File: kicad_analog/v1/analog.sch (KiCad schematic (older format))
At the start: 9 parts, among them J1 Conn_01x03, J2 Conn_02x05_Odd_Even, J3 Conn_02x05_Odd_Even, U1 BH2220FVM, U2 TSV994, U3 TSV994

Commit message: Add rough layout of components for 3d pcb view
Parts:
- J2: footprint Connector_PinSocket_2.54mm:PinSocket_2x05_P2.54mm_Vertical -> Connector_PinHeader_2.54mm:PinHeader_2x05_P2.54mm_Horizontal
- J3: footprint Connector_PinSocket_2.54mm:PinSocket_2x05_P2.54mm_Vertical -> Connector_PinSocket_2.54mm:PinSocket_2x05_P2.54mm_Horizontal
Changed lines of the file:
@@
 F 0 "J2" H 2150 3567 50  0000 C CNN
 F 1 "Conn_02x05_Odd_Even" H 2150 3476 50  0000 C CNN
-F 2 "Connector_PinSocket_2.54mm:PinSocket_2x05_P2.54mm_Vertical" H 2100 3150 50  0001 C CNN
+F 2 "Connector_PinHeader_2.54mm:PinHeader_2x05_P2.54mm_Horizontal" H 2100 3150 50  0001 C CNN
 F 3 "~" H 2100 3150 50  0001 C CNN
 	1    2100 3150
@@
 F 0 "J3" H 10100 3667 50  0000 C CNN
 F 1 "Conn_02x05_Odd_Even" H 10100 3576 50  0000 C CNN
-F 2 "Connector_PinSocket_2.54mm:PinSocket_2x05_P2.54mm_Vertical" H 10050 3250 50  0001 C CNN
+F 2 "Connector_PinSocket_2.54mm:PinSocket_2x05_P2.54mm_Horizontal" H 10050 3250 50  0001 C CNN
 F 3 "~" H 10050 3250 50  0001 C CNN
 	1    10050 3250

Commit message: Analog board updated with MAX9201, terminators and rough pcb layout
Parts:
- removed J2: Conn_02x05_Odd_Even, Connector_PinHeader_2.54mm:PinHeader_2x05_P2.54mm_Horizontal, symbol Connector_Generic:Conn_02x05_Odd_Even
- removed U2, U3: TSV994, Package_SO:SOIC-14_3.9x8.7mm_P1.27mm, symbol Amplifier_Operational:TSV994
- added J2: Conn_01x05, Connector_PinHeader_2.54mm:PinHeader_1x05_P2.54mm_Horizontal, symbol Connector_Generic:Conn_01x05
- added RN1: 75R, Resistor_THT:R_Array_SIP6, symbol Device:R_Network04
- added U2, U3: MAX9201, Package_SO:TSSOP-16_4.4x5mm_P0.65mm, symbol Comparator:MAX9201
- J1: footprint Connector_PinHeader_2.54mm:PinHeader_1x03_P2.54mm_Vertical -> Connector_PinHeader_2.54mm:PinHeader_1x03_P2.54mm_Horizontal
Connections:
- net labels removed: AVSYNC
- wire segments 60 -> 64
- no-connect marks 3 -> 0
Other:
- moved on the sheet: J3

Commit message: Change DAC and use VSYNC as monochrome video input (requires V6.5 CPLD)
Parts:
- removed U1: BH2220FVM, Package_SO:MSOP-8_3x3mm_P0.65mm, symbol analog-rescue:BH2220FVM-bh2220fvm
- added U1: DAC084S085, Package_SO:VSSOP-10_3x3mm_P0.5mm, symbol Analog_DAC:DAC084S085
- RN1: value 75R -> R_Network04; footprint Resistor_THT:R_Array_SIP6 -> Resistor_THT:R_Array_SIP5
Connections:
- wire segments 64 -> 67
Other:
- note added: "Monochrome ref"
- moved on the sheet: J1, J3, U2A, U2B, U2C, U2D, U3A, U3B, U3C, U3D

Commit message: All tracks routed on analog board
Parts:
- removed C1, C2, C3: CAP, Capacitor_SMD:C_0805_2012Metric_Pad1.15x1.40mm_HandSolder, symbol pspice:CAP
- removed RN1: R_Network04, Resistor_THT:R_Array_SIP5, symbol Device:R_Network04
- added C1: 10uF, Capacitor_SMD:C_0805_2012Metric_Pad1.15x1.40mm_HandSolder, symbol Device:C_Small
- added C2, C3, C4, C5: 100n, Capacitor_SMD:C_0805_2012Metric_Pad1.15x1.40mm_HandSolder, symbol Device:C_Small
- added JP1: Jumper, Jumper:SolderJumper-2_P1.3mm_Open_RoundedPad1.0x1.5mm, symbol Device:Jumper
- added R1, R2, R3, R4: 75R, Resistor_SMD:R_0805_2012Metric_Pad1.15x1.40mm_HandSolder, symbol Device:R_Small
- added RX1: 0R, Resistor_SMD:R_0805_2012Metric_Pad1.15x1.40mm_HandSolder, symbol Device:R_Small
- added U4: MCP1754-3302E_SOT89, Package_TO_SOT_SMD:SOT-89-3, symbol Regulator_Linear:MCP1754-3302E_SOT89
- J1: footprint Connector_PinHeader_2.54mm:PinHeader_1x03_P2.54mm_Horizontal -> Connector_PinHeader_2.54mm:PinHeader_1x03_P2.54mm_Vertical
- J2: footprint Connector_PinHeader_2.54mm:PinHeader_1x05_P2.54mm_Horizontal -> Connector_Molex:Molex_PicoBlade_53048-0510_1x05_P1.25mm_Horizontal
- U2, U3: footprint Package_SO:TSSOP-16_4.4x5mm_P0.65mm -> Package_SO:SOIC-16_3.9x9.9mm_P1.27mm
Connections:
- net labels added: REF100, REF50, REFMONO, REFSYNC, VANALOG
- wire segments 67 -> 106
- no-connect marks 0 -> 2
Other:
- note removed: "100% ref"
- note removed: "50% ref"
- note removed: "Monochrome ref"
- note removed: "Sync ref"
- moved on the sheet: J1, J2, J3, U1, U2A, U2B, U2C, U2D, U2E, U3A, U3B, U3C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

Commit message: Add JP2, J4 & Groundplane
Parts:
- added J4: Conn_01x02, Connector_PinHeader_2.54mm:PinHeader_1x02_P2.54mm_Vertical, symbol Connector_Generic:Conn_01x02
- added JP2: SolderJumper_2_Open, Jumper:SolderJumper-2_P1.3mm_Open_RoundedPad1.0x1.5mm, symbol Jumper:SolderJumper_2_Open
- renumbered RX1 to SPACER1
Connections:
- net ASYNC: now also J4.2 (Pin_2)
- net GND: now also J4.1 (Pin_1)
- net VANALOG: now also JP2.2 (B)
- net VCC: now also JP2.1 (A)
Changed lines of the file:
@@
 	1650 2350 1750 2350
 Wire Wire Line
-	1750 2350 1750 3400
+	1750 2350 1750 2650
 Wire Wire Line
 	1750 3400 2050 3400
@@
 	5200 6750 5550 6750
 Wire Wire Line
-	2050 5700 4000 5700
+	2050 5700 3600 5700
 Wire Wire Line
 	2050 6200 4300 6200
 Wire Wire Line
-	4600 5700 5400 5700
+	4600 5700 4950 5700
 Wire Wire Line
 	4300 6200 5400 6200
 $Comp
-L Device:R_Small RX1
+L Device:R_Small SPACER1
 U 1 1 5DD9AF8A
 P 2050 1100
-F 0 "RX1" H 2109 1146 50  0000 L CNN
+F 0 "SPACER1" H 2109 1146 50  0000 L CNN
 F 1 "0R" H 2109 1055 50  0000 L CNN
 F 2 "Resistor_SMD:R_0805_2012Metric_Pad1.15x1.40mm_HandSolder" H 2050 1100 50  0001 C CNN
@@
 $EndComp
 Wire Wire Line
-	1650 2250 2050 2250
+	1650 2250 1850 2250
 Wire Wire Line
 	2050 2400 2050 2250
@@
 Wire Wire Line
 	2050 2250 3350 2250
+$Comp
+L Jumper:SolderJumper_2_Open JP2
+U 1 1 5DCD15F3
+P 4300 5350
+F 0 "JP2" H 4300 5555 50  0000 C CNN
+F 1 "SolderJumper_2_Open" H 4300 5464 50  0000 C CNN
+F 2 "Jumper:SolderJumper-2_P1.3mm_Open_RoundedPad1.0x1.5mm" H 4300 5350 50  0001 C CNN
+F 3 "~" H 4300 5350 50  0001 C CNN
+	1    4300 5350
+	1    0    0    -1
+$EndComp
+Wire Wire Line
+	4450 5350 4950 5350
+Wire Wire Line
+	4950 5350 4950 5700
+Connection ~ 4950 5700
+Wire Wire Line
+	4950 5700 5400 5700
+Wire Wire Line
+	4150 5350 3600 5350
+Wire Wire Line
+	3600 5350 3600 5700
+Connection ~ 3600 5700
+Wire Wire Line
+	3600 5700 4000 5700
+$Comp
+L Connector_Generic:Conn_01x02 J4
+U 1 1 5DD175CA
+P 1450 2650
+F 0 "J4" H 1650 2650 50  0000 C CNN
+F 1 "Conn_01x02" H 1800 2550 50  0000 C CNN
+F 2 "Connector_PinHeader_2.54mm:PinHeader_1x02_P2.54mm_Vertical" H 1450 2650 50  0001 C CNN
+F 3 "~" H 1450 2650 50  0001 C CNN
+	1    1450 2650
+	-1   0    0    1
+$EndComp
+Wire Wire Line
+	1650 2650 1750 2650
+Connection ~ 1750 2650
+Wire Wire Line
+	1750 2650 1750 3400
+Wire Wire Line
+	1650 2550 1850 2550
+Wire Wire Line
+	1850 2550 1850 2250
+Connection ~ 1850 2250
+Wire Wire Line
+	1850 2250 2050 2250
 $EndSCHEMATC

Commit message: Move 3 pin data header + add silk screen
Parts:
- removed JP1: Jumper, Jumper:SolderJumper-2_P1.3mm_Open_RoundedPad1.0x1.5mm, symbol Device:Jumper
- removed SPACER1: 0R, Resistor_SMD:R_0805_2012Metric_Pad1.15x1.40mm_HandSolder, symbol Device:R_Small
- added J5, J6: Conn_01x01, Connector_PinHeader_2.54mm:PinHeader_1x01_P2.54mm_Vertical, symbol Connector_Generic:Conn_01x01
- added JP1: SolderJumper_2_Bridged, Jumper:SolderJumper-2_P1.3mm_Bridged_RoundedPad1.0x1.5mm, symbol Jumper:SolderJumper_2_Bridged
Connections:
- net ASYNC: now also JP1.1 (A)
- net at R1.1: now also JP1.2 (B)
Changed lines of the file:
@@
 Wire Wire Line
 	4300 6200 5400 6200
-$Comp
-L Device:R_Small SPACER1
-U 1 1 5DD9AF8A
-P 2050 1100
-F 0 "SPACER1" H 2109 1146 50  0000 L CNN
-F 1 "0R" H 2109 1055 50  0000 L CNN
-F 2 "Resistor_SMD:R_0805_2012Metric_Pad1.15x1.40mm_HandSolder" H 2050 1100 50  0001 C CNN
-F 3 "~" H 2050 1100 50  0001 C CNN
-	1    2050 1100
-	1    0    0    -1
-$EndComp
-NoConn ~ 2050 1000
-NoConn ~ 2050 1200
-$Comp
-L Device:Jumper JP1
-U 1 1 5DDAE5B6
-P 2050 2700
-F 0 "JP1" V 2096 2612 50  0000 R CNN
-F 1 "Jumper" V 2005 2612 50  0000 R CNN
-F 2 "Jumper:SolderJumper-2_P1.3mm_Open_RoundedPad1.0x1.5mm" H 2050 2700 50  0001 C CNN
-F 3 "~" H 2050 2700 50  0001 C CNN
-	1    2050 2700
-	0    -1   -1   0
-$EndComp
 Wire Wire Line
 	1650 2250 1850 2250
-Wire Wire Line
-	2050 2400 2050 2250
-Connection ~ 2050 2250
-Wire Wire Line
-	2050 2250 3350 2250
 $Comp
 L Jumper:SolderJumper_2_Open JP2
@@
 	1850 2550 1850 2250
 Connection ~ 1850 2250
+$Comp
+L Jumper:SolderJumper_2_Bridged JP1
+U 1 1 5DCCD072
+P 2050 2700
+F 0 "JP1" V 2004 2768 50  0000 L CNN
+F 1 "SolderJumper_2_Bridged" V 2095 2768 50  0000 L CNN
+F 2 "Jumper:SolderJumper-2_P1.3mm_Bridged_RoundedPad1.0x1.5mm" H 2050 2700 50  0001 C CNN
+F 3 "~" H 2050 2700 50  0001 C CNN
+	1    2050 2700
+	0    1    1    0
+$EndComp
 Wire Wire Line
 	1850 2250 2050 2250
+Wire Wire Line
+	2050 2550 2050 2250
+Connection ~ 2050 2250
+Wire Wire Line
+	2050 2250 3350 2250
+Wire Wire Line
+	2050 2850 2050 3000
+$Comp
+L Connector_Generic:Conn_01x01 J6
+U 1 1 5DD07D72
+P 1100 850
+F 0 "J6" H 1180 892 50  0000 L CNN
+F 1 "Conn_01x01" H 1180 801 50  0000 L CNN
+F 2 "Connector_PinHeader_2.54mm:PinHeader_1x01_P2.54mm_Vertical" H 1100 850 50  0001 C CNN
+F 3 "~" H 1100 850 50  0001 C CNN
+	1    1100 850
+	1    0    0    -1
+$EndComp
+$Comp
+L Connector_Generic:Conn_01x01 J5
+U 1 1 5DD08736
+P 1100 1200
+F 0 "J5" H 1180 1242 50  0000 L CNN
+F 1 "Conn_01x01" H 1180 1151 50  0000 L CNN
+F 2 "Connector_PinHeader_2.54mm:PinHeader_1x01_P2.54mm_Vertical" H 1100 1200 50  0001 C CNN
+F 3 "~" H 1100 1200 50  0001 C CNN
+	1    1100 1200
+	1    0    0    -1
+$EndComp
+NoConn ~ 900  850
+NoConn ~ 900  1200
 $EndSCHEMATC

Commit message: Add P19 pin and new jumpers
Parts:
- removed J1: Conn_01x03, Connector_PinHeader_2.54mm:PinHeader_1x03_P2.54mm_Vertical, symbol Connector_Generic:Conn_01x03
- added JP3: SolderJumper_3_Bridged12, Jumper:SolderJumper-3_P1.3mm_Bridged12_RoundedPad1.0x1.5mm, symbol Jumper:SolderJumper_3_Bridged12
- added P2: Conn_01x04, Connector_PinHeader_2.54mm:PinHeader_1x04_P2.54mm_Vertical, symbol Connector_Generic:Conn_01x04
- renumbered J3 to P1, J2 to P3, J4 to P4, J5 to P5, J6 to P6
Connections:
- net GPIO0: now also P2.1 (Pin_1)
- net GPIO20: now also P2.2 (Pin_2)
- net GPIO22: now also P2.3 (Pin_3)
- net VANALOG: now also JP3.3 (B)
- net VCC: now also JP3.1 (A); no longer U1.1 (VA)
- new net: JP3.2 (C), U1.1 (VA)
- new net P19: P2.4 (Pin_4)
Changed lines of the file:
@@
 $EndDescr
 $Comp
-L Connector_Generic:Conn_02x05_Odd_Even J3
+L Connector_Generic:Conn_02x05_Odd_Even P1
 U 1 1 5DB26BD3
 P 10150 2700
-F 0 "J3" H 10200 3117 50  0000 C CNN
+F 0 "P1" H 10200 3117 50  0000 C CNN
 F 1 "Conn_02x05_Odd_Even" H 10200 3026 50  0000 C CNN
 F 2 "Connector_PinSocket_2.54mm:PinSocket_2x05_P2.54mm_Horizontal" H 10150 2700 50  0001 C CNN
@@
 Text Label 9950 2500 2    50   ~ 0
 VCC
-Text Label 2500 4450 2    50   ~ 0
-VCC
 Text Label 2500 5050 2    50   ~ 0
 GND
 Text Label 3000 7450 2    50   ~ 0
 GND
-$Comp
-L Connector_Generic:Conn_01x03 J1
-U 1 1 5DB1E4F3
-P 1300 4750
-F 0 "J1" H 1218 5067 50  0000 C CNN
-F 1 "Conn_01x03" H 1218 4976 50  0000 C CNN
-F 2 "Connector_PinHeader_2.54mm:PinHeader_1x03_P2.54mm_Vertical" H 1300 4750 50  0001 C CNN
-F 3 "~" H 1300 4750 50  0001 C CNN
-	1    1300 4750
-	-1   0    0    -1
-$EndComp
 Wire Wire Line
 	1500 4750 2500 4750
@@
 BLUE
 $Comp
-L Connector_Generic:Conn_01x05 J2
+L Connector_Generic:Conn_01x05 P3
 U 1 1 5DC7AFF6
 P 1450 2150
-F 0 "J2" H 1530 2192 50  0000 L CNN
+F 0 "P3" H 1530 2192 50  0000 L CNN
 F 1 "Conn_01x05" H 1530 2101 50  0000 L CNN
 F 2 "Connector_Molex:Molex_PicoBlade_53048-0510_1x05_P1.25mm_Horizontal" H 1450 2150 50  0001 C CNN
@@
 	3600 5700 4000 5700
 $Comp
-L Connector_Generic:Conn_01x02 J4
+L Connector_Generic:Conn_01x02 P4
 U 1 1 5DD175CA
 P 1450 2650
-F 0 "J4" H 1650 2650 50  0000 C CNN
+F 0 "P4" H 1650 2650 50  0000 C CNN
 F 1 "Conn_01x02" H 1800 2550 50  0000 C CNN
 F 2 "Connector_PinHeader_2.54mm:PinHeader_1x02_P2.54mm_Vertical" H 1450 2650 50  0001 C CNN
@@
 	2050 2850 2050 3000
 $Comp
-L Connector_Generic:Conn_01x01 J6
+L Connector_Generic:Conn_01x01 P6
 U 1 1 5DD07D72
 P 1100 850
-F 0 "J6" H 1180 892 50  0000 L CNN
+F 0 "P6" H 1180 892 50  0000 L CNN
 F 1 "Conn_01x01" H 1180 801 50  0000 L CNN
 F 2 "Connector_PinHeader_2.54mm:PinHeader_1x01_P2.54mm_Vertical" H 1100 850 50  0001 C CNN
@@
 $EndComp
 $Comp
-L Connector_Generic:Conn_01x01 J5
+L Connector_Generic:Conn_01x01 P5
 U 1 1 5DD08736
 P 1100 1200
-F 0 "J5" H 1180 1242 50  0000 L CNN
+F 0 "P5" H 1180 1242 50  0000 L CNN
 F 1 "Conn_01x01" H 1180 1151 50  0000 L CNN
 F 2 "Connector_PinHeader_2.54mm:PinHeader_1x01_P2.54mm_Vertical" H 1100 1200 50  0001 C CNN
@@
 NoConn ~ 900  850
 NoConn ~ 900  1200
+$Comp
+L Connector_Generic:Conn_01x04 P2
+U 1 1 5DCFA861
+P 1300 4750
+F 0 "P2" H 1218 4325 50  0000 C CNN
+F 1 "Conn_01x04" H 1218 4416 50  0000 C CNN
+F 2 "Connector_PinHeader_2.54mm:PinHeader_1x04_P2.54mm_Vertical" H 1300 4750 50  0001 C CNN
+F 3 "~" H 1300 4750 50  0001 C CNN
+	1    1300 4750
+	-1   0    0    1
+$EndComp
+Text Label 1500 4550 0    50   ~ 0
+P19
+$Comp
+L Jumper:SolderJumper_3_Bridged12 JP3
+U 1 1 5DD662E2
+P 2400 3900
+F 0 "JP3" H 2400 4105 50  0000 C CNN
+F 1 "SolderJumper_3_Bridged12" H 2400 4014 50  0000 C CNN
+F 2 "Jumper:SolderJumper-3_P1.3mm_Bridged12_RoundedPad1.0x1.5mm" H 2400 3900 50  0001 C CNN
+F 3 "~" H 2400 3900 50  0001 C CNN
+	1    2400 3900
+	1    0    0    -1
+$EndComp
+Text Label 2200 3900 2    50   ~ 0
+VCC
+Text Label 2600 3900 0    50   ~ 0
+VANALOG
+Wire Wire Line
+	2500 4450 2400 4450
+Wire Wire Line
+	2400 4450 2400 4050
 $EndSCHEMATC

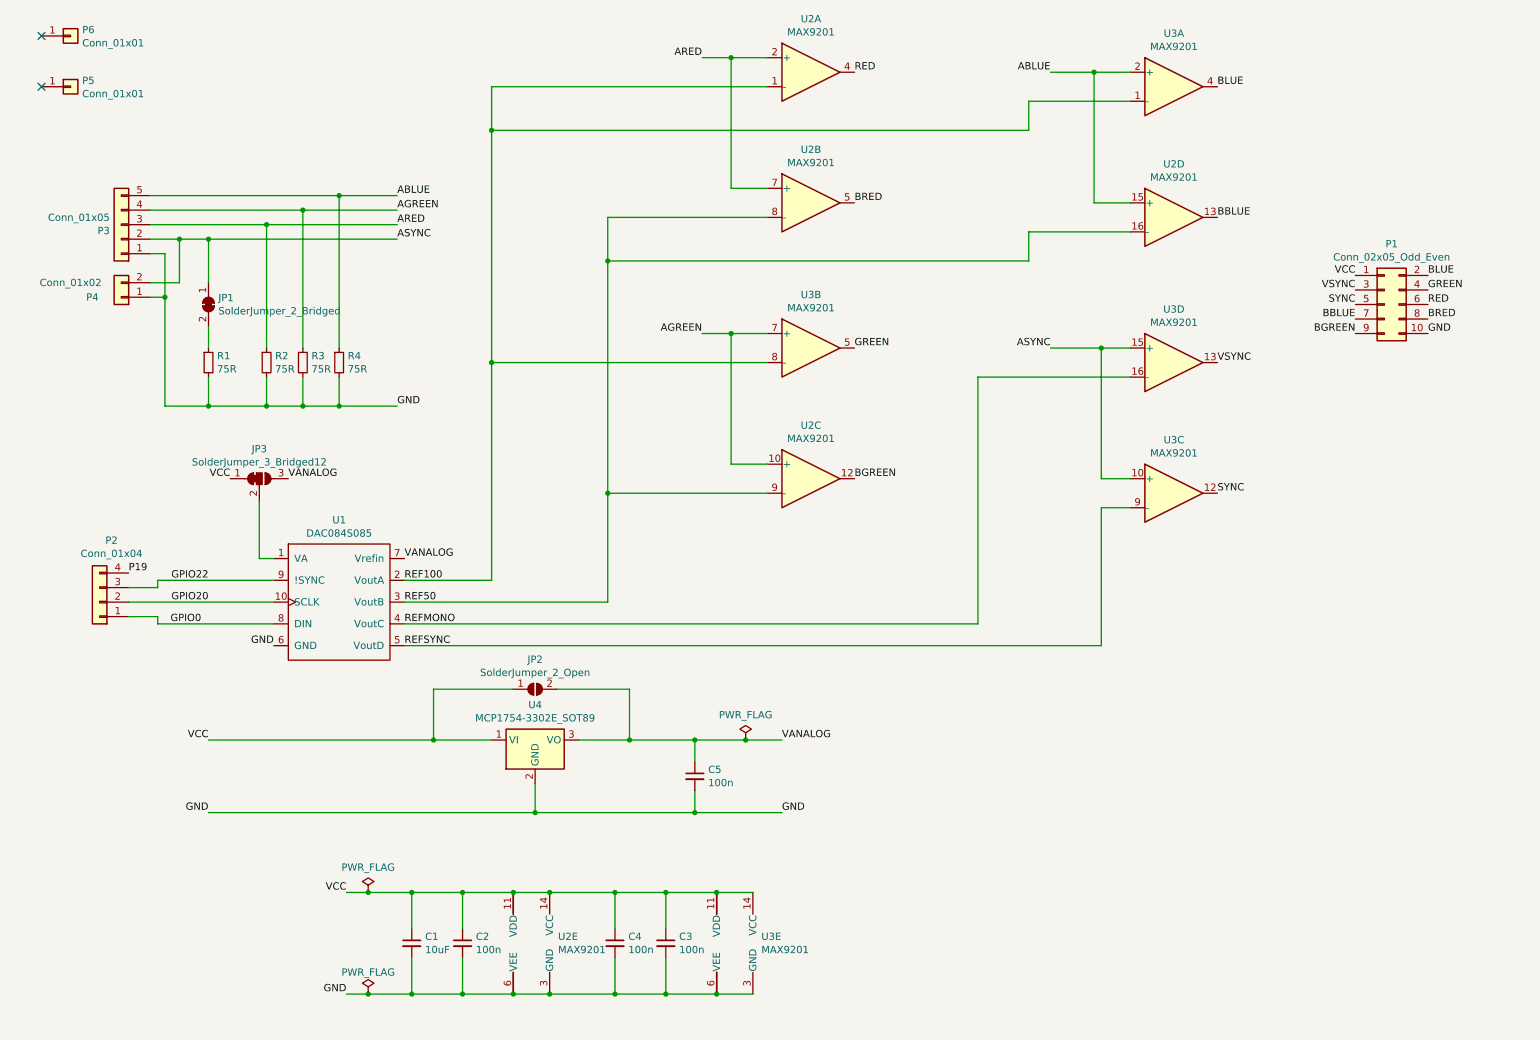
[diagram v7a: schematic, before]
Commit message: Change DAC to TLC5620 and add software controllable termination
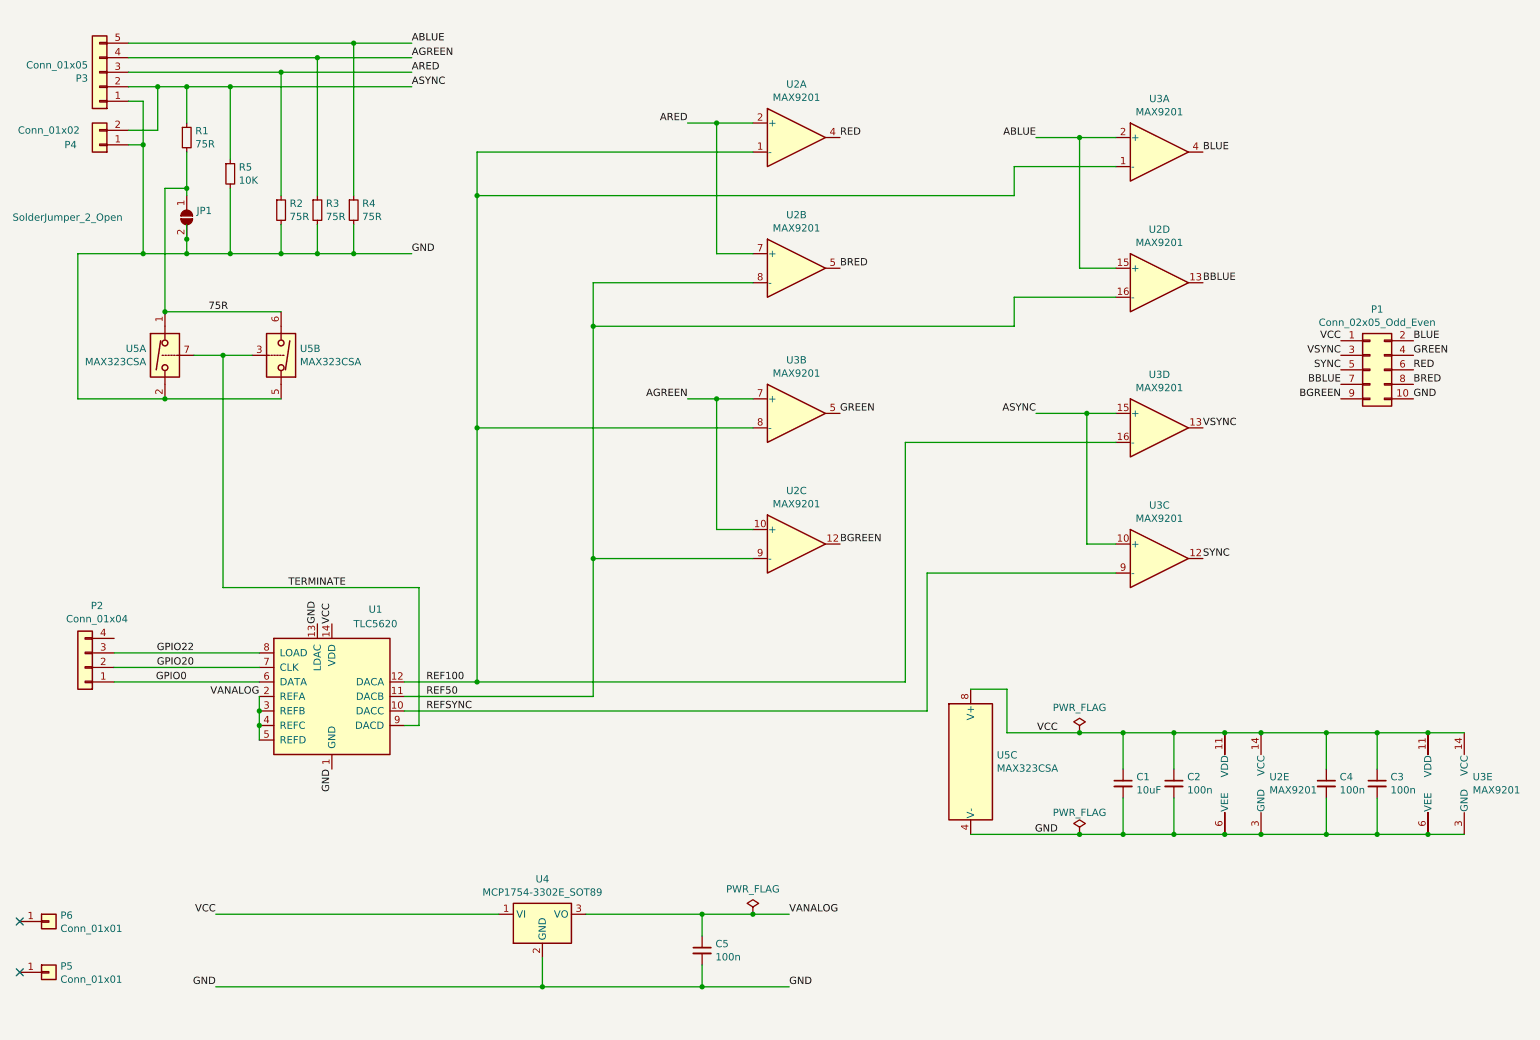
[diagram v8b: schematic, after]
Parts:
- removed JP1: SolderJumper_2_Bridged, Jumper:SolderJumper-2_P1.3mm_Bridged_RoundedPad1.0x1.5mm, symbol Jumper:SolderJumper_2_Bridged
- removed JP2: SolderJumper_2_Open, Jumper:SolderJumper-2_P1.3mm_Open_RoundedPad1.0x1.5mm, symbol Jumper:SolderJumper_2_Open
- removed JP3: SolderJumper_3_Bridged12, Jumper:SolderJumper-3_P1.3mm_Bridged12_RoundedPad1.0x1.5mm, symbol Jumper:SolderJumper_3_Bridged12
- removed U1: DAC084S085, Package_SO:VSSOP-10_3x3mm_P0.5mm, symbol Analog_DAC:DAC084S085
- added JP1: SolderJumper_2_Open, Jumper:SolderJumper-2_P1.3mm_Open_RoundedPad1.0x1.5mm, symbol Jumper:SolderJumper_2_Open
- added R5: 10K, Resistor_SMD:R_0805_2012Metric_Pad1.15x1.40mm_HandSolder, symbol Device:R_Small
- added U1: TLC5620, Package_SO:SOIC-14_3.9x8.7mm_P1.27mm, symbol Analog_DAC:TLC5620
- added U5: MAX323CSA, Package_SO:SOIC-8_3.9x4.9mm_P1.27mm, symbol Analog_Switch:MAX323CSA
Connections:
- net REFMONO is gone; now on net REF100: U3.16 (-)
- net ASYNC: now also R1.1, R5.1
- net GND: now also JP1.2 (B), R5.2, U1.1 (GND), U1.13 (LDAC), U5.2, U5.4 (V-), U5.5; no longer R1.2
- net GPIO0: now also U1.6 (DATA)
- net GPIO20: now also U1.7 (CLK)
- net GPIO22: now also U1.8 (LOAD)
- net REF100: now also U1.12 (DACA)
- net REF50: now also U1.11 (DACB)
- net REFSYNC: now also U1.10 (DACC)
- net VANALOG: now also U1.2 (REFA), U1.3 (REFB), U1.4 (REFC), U1.5 (REFD)
- net VCC: now also U1.14 (VDD), U5.8 (V+)
- net P19: no longer names the net of P2.4 (Pin_4)
- new net 75R: JP1.1 (A), R1.2, U5.1, U5.6
- new net TERMINATE: U1.9 (DACD), U5.3, U5.7
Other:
- moved on the sheet: C1, C2, C3, C4, C5, P1, P2, P3, P4, P5, P6, R1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
